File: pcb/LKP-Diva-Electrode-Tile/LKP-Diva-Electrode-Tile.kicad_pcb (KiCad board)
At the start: 2 copper layers, 258 x 40 mm, 19 parts, among them J1 Intercon, J10 Electrode 1, J11 Electrode 3, J12 Electrode 5, J13 Electrode 7, J14 Electrode 9, J15 Electrode 11, J16 Electrode 13, J17 Electrode 15, J2 Electrode 0, J3 Electrode 2, J4 Electrode 4, J5 Electrode 6, J6 Electrode 8, J7 Electrode 10, J8 Electrode 12, J9 Electrode 14

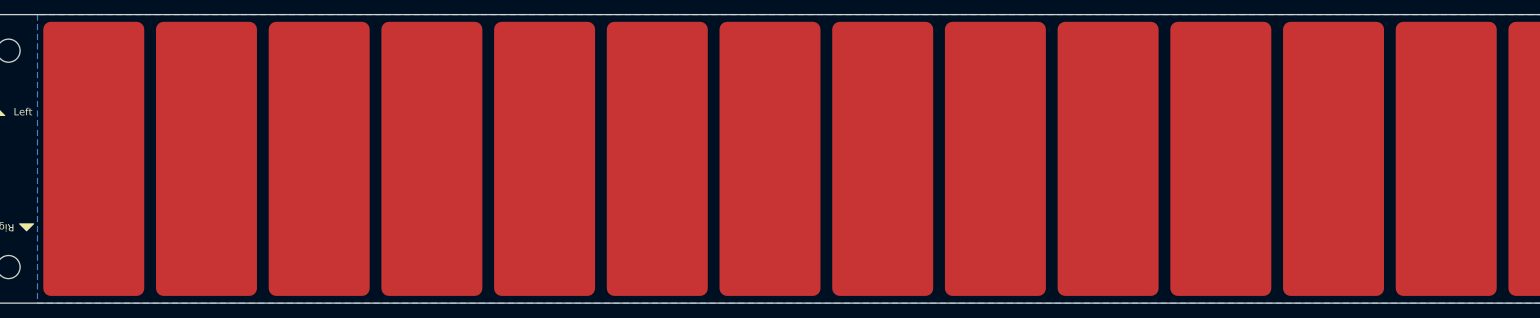
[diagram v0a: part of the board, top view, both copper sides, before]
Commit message: Fix sensor topology
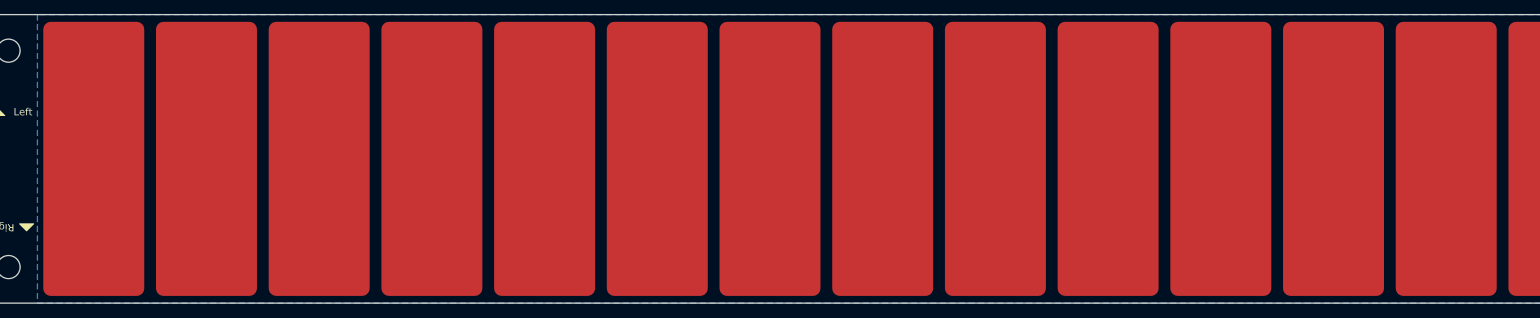
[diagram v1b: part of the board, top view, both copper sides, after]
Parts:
- J10: value Electrode 1 -> Electrode 0
- J11: value Electrode 3 -> Electrode 2
- J12: value Electrode 5 -> Electrode 4
- J13: value Electrode 7 -> Electrode 6
- J14: value Electrode 9 -> Electrode 8
- J15: value Electrode 11 -> Electrode 10
- J16: value Electrode 13 -> Electrode 12
- J17: value Electrode 15 -> Electrode 14
- J2: value Electrode 0 -> Electrode 1
- J3: value Electrode 2 -> Electrode 3
- J4: value Electrode 4 -> Electrode 5
- J5: value Electrode 6 -> Electrode 7
- J6: value Electrode 8 -> Electrode 9
- J7: value Electrode 10 -> Electrode 11
- J8: value Electrode 12 -> Electrode 13
- J9: value Electrode 14 -> Electrode 15
- moved J10 15.6 mm to (39.1, 104.0)
- moved J11 15.6 mm to (70.3, 104.0)
- moved J13 15.6 mm to (132.8, 104.0)
- moved J16 15.6 mm to (226.6, 104.0)
- moved J17 15.6 mm to (257.8, 104.0)
- moved J12 15.6 mm to (101.6, 104.0)
- moved J14 15.6 mm to (164.1, 104.0)
- moved J15 15.6 mm to (195.3, 104.0)
- moved J9 15.6 mm to (273.4, 104.0)
- moved J8 15.6 mm to (242.2, 104.0)
- moved J7 15.6 mm to (210.9, 104.0)
- moved J6 15.6 mm to (179.7, 104.0)
- moved J5 15.6 mm to (148.4, 104.0)
- moved J4 15.6 mm to (117.2, 104.0)
- moved J3 15.6 mm to (85.9, 104.0)
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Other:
- board text removed: "Left Side"

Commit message: Iteration 1.1 routing
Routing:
- net Net-(J1-Pad2): track 0.00 -> 223.4 mm, vias 0 -> 1
- net Net-(J1-Pad3): track 0.00 -> 201.9 mm, vias 0 -> 1
- net Net-(J1-Pad4): track 0.00 -> 192.2 mm, vias 0 -> 1
- net Net-(J1-Pad5): track 0.00 -> 170.7 mm, vias 0 -> 1
- net Net-(J1-Pad6): track 0.00 -> 160.9 mm, vias 0 -> 1
- net Net-(J1-Pad7): track 0.00 -> 139.5 mm, vias 0 -> 1
- net Net-(J1-Pad8): track 0.00 -> 129.7 mm, vias 0 -> 1
- net Net-(J1-Pad9): track 0.00 -> 108.2 mm, vias 0 -> 1
- net Net-(J1-Pad10): track 0.00 -> 98.4 mm, vias 0 -> 1
- net Net-(J1-Pad11): track 0.00 -> 77.0 mm, vias 0 -> 1
- net Net-(J1-Pad12): track 0.00 -> 67.2 mm, vias 0 -> 1
- net Net-(J1-Pad13): track 0.00 -> 45.5 mm, vias 0 -> 1
- net Net-(J1-Pad14): track 0.00 -> 35.9 mm, vias 0 -> 1
- net Net-(J1-Pad15): track 0.00 -> 14.5 mm, vias 0 -> 1
- net Net-(J1-Pad16): track 0.00 -> 8.51 mm, vias 0 -> 1
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- added copper zone on F.Cu, net GNDA
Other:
- net class CapSense: clearance 0.4 -> 0.25
